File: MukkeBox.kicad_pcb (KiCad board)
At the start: 2 copper layers, 200 x 105 mm, 273 parts, among them J101 Conn_02x20_Odd_Even, J102 Conn_01x04, J103 Conn_02x05_Odd_Even, J104 Conn_02x05_Odd_Even, J201 Conn_02x01, J301 Conn_02x04_Odd_Even, J302 Conn_02x04_Odd_Even, J303 TB001-500-02BE CUI_Devices, J401 TB001-500-02BE CUI_Devices, J501 TB001-500-04BE CUI_Devices, J601 Conn_01x03_Female, J602 Conn_02x01, J603 Conn_02x06_Odd_Even, J604 Conn_02x01, J605 Conn_02x01, Q1 2N7002, Q303 2N7002, Q304 2N7002, Q305 FDD4685-F085, Q306 2N7002, Q307 BSS84, Q308 2N7002, Q309 FDD4685-F085, Q401 2N7002, Q402 2N7002, Q501 2N7002, SW501 DS04-254-2-02BK-SMT, U101 LM35-LP, U102 STM32F030C6Tx_MukkeBox, U201 XC6216C, U202 StepUp, U401 MAX1873TEEE, U501 TDA7498L, U502 BK8000L, U503 TDA7719, U504 AP2553AW6-7, U601 XC6216C, U602 TPS560430, Y101 FOXSDLF/080-20

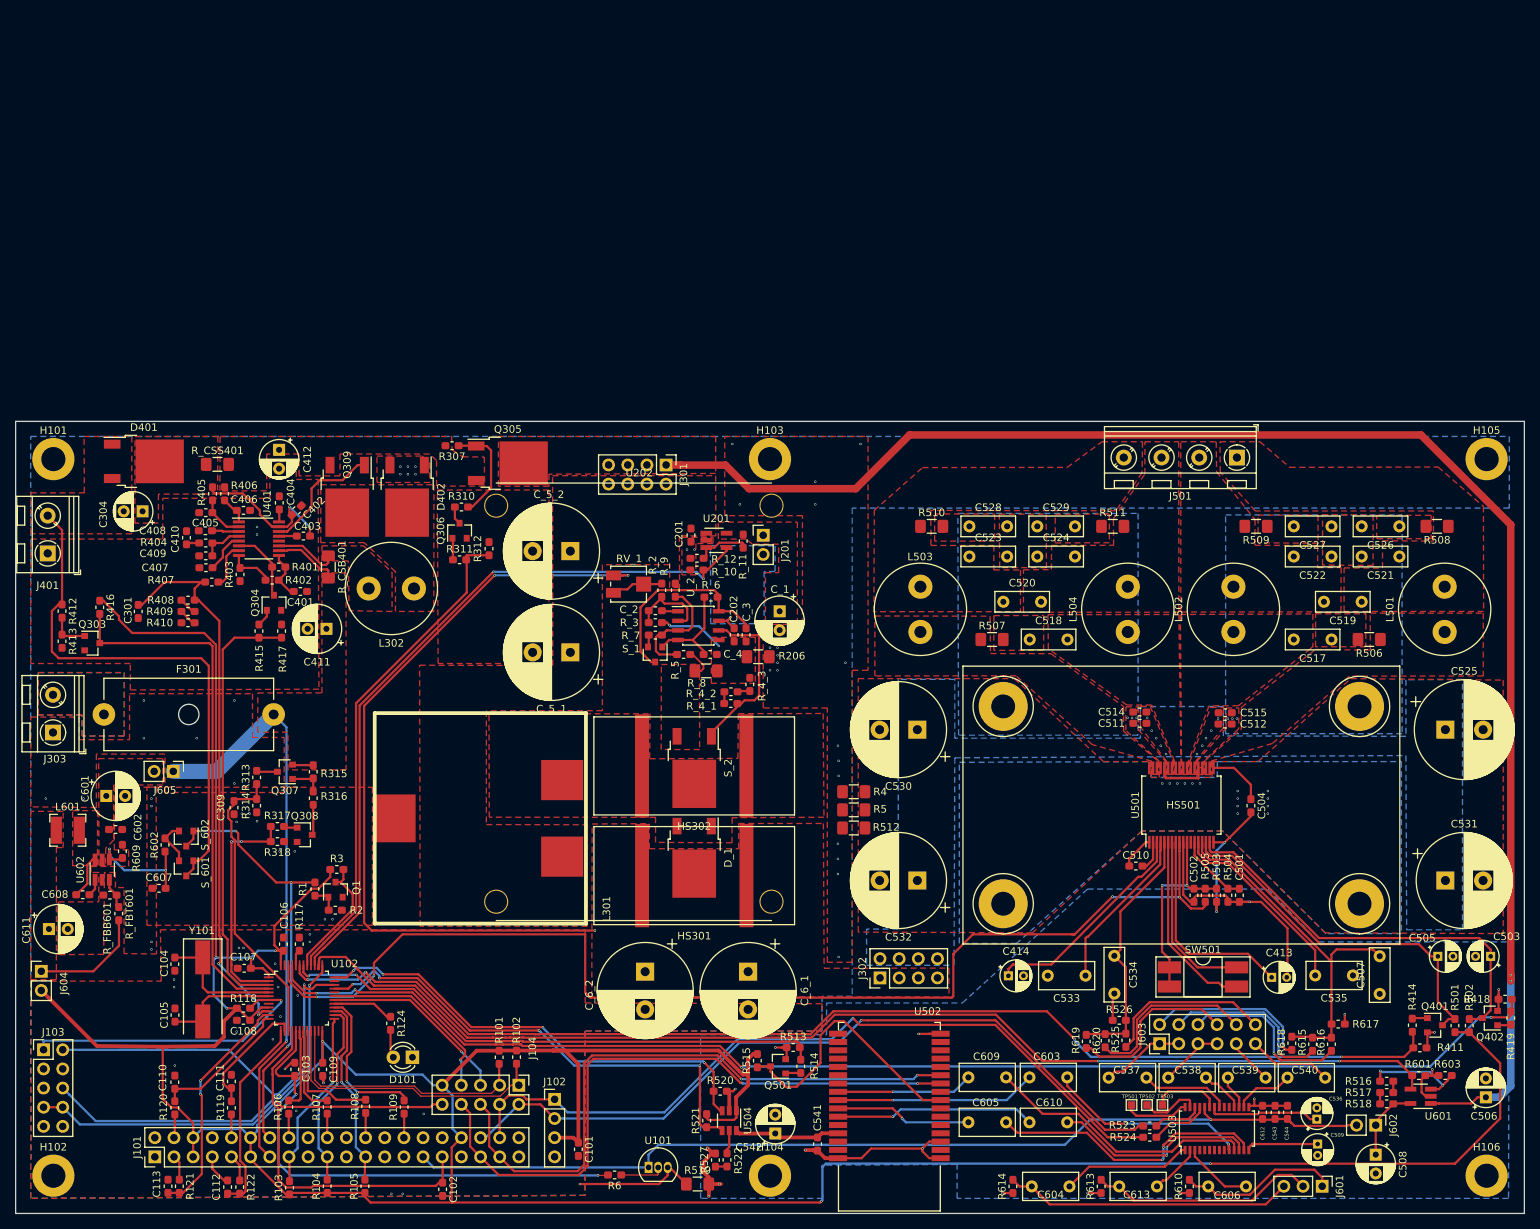
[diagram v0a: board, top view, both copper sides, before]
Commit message: Charger austauschen gegen bq24610
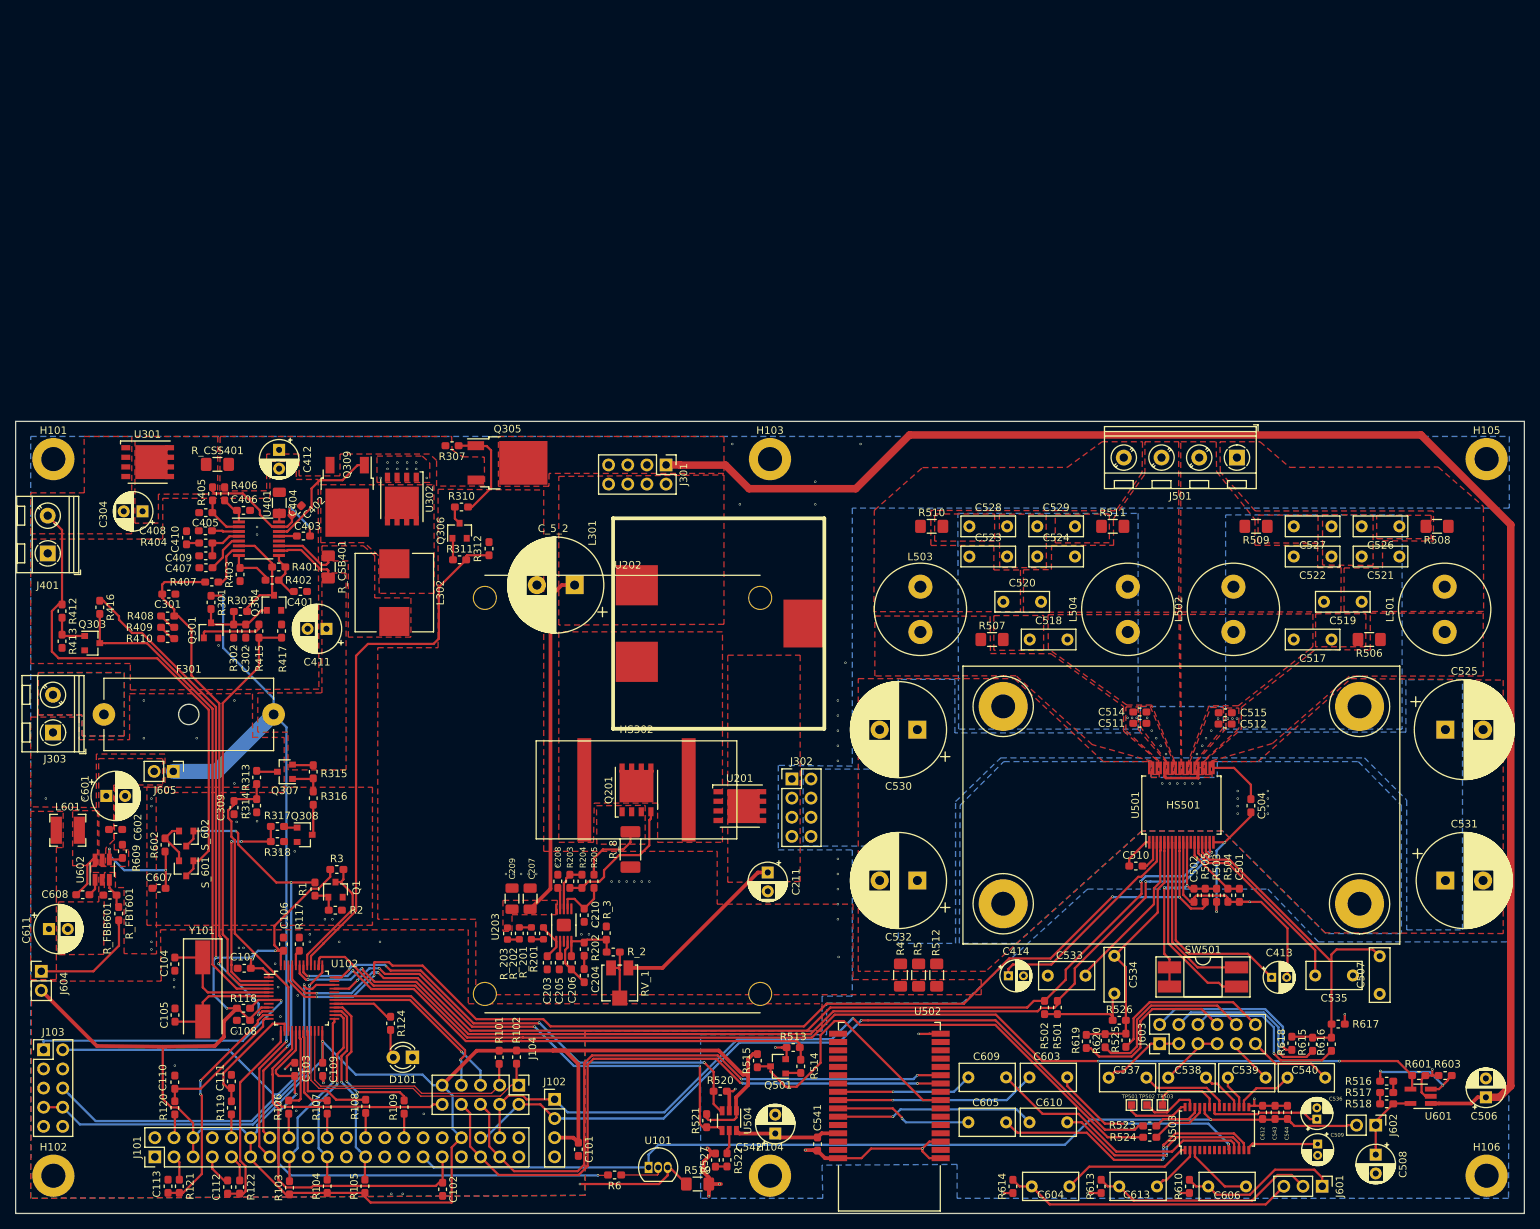
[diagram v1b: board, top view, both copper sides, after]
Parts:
- removed C201, C202: 100n, Capacitor_SMD:C_0603_1608Metric_Pad1.05x0.95mm_HandSolder
- removed C503, C505: 2.2uF 16V, Capacitor_THT:CP_Radial_D4.0mm_P2.00mm
- removed C_1: 68u, Capacitor_THT:CP_Radial_D6.3mm_P2.50mm
- removed C_2: 100nF, Capacitor_SMD:C_0603_1608Metric_Pad1.05x0.95mm_HandSolder
- removed C_3: 220nF, Capacitor_SMD:C_0603_1608Metric_Pad1.05x0.95mm_HandSolder
- removed C_4: 1.2nF, Capacitor_SMD:C_0603_1608Metric_Pad1.05x0.95mm_HandSolder
- removed C_5_1, C_6_1, C_6_2: 560uF 50V, Capacitor_THT:CP_Radial_D12.5mm_P5.00mm
- removed D401, D402, D_1: STPS1045B-TR, Package_TO_SOT_SMD:TO-252-2
- removed HS301: 573300D00000G, Heatsink:Heatsink_AAVID_573300D00010G_TO-263
- removed J201: Conn_02x01, Connector_PinHeader_2.54mm:PinHeader_1x02_P2.54mm_Vertical
- removed Q401, Q402: 2N7002, Package_TO_SOT_SMD:SOT-23
- removed R206: 0R, Resistor_SMD:R_1206_3216Metric_Pad1.42x1.75mm_HandSolder
- removed R411, R418, R_9: 100K, Resistor_SMD:R_0603_1608Metric_Pad1.05x0.95mm_HandSolder
- removed R414, R419, R_5: 1K, Resistor_SMD:R_0603_1608Metric_Pad1.05x0.95mm_HandSolder
- removed R_10, R_12, R_4_1, R_4_2, R_4_3: 10K, Resistor_SMD:R_0603_1608Metric_Pad1.05x0.95mm_HandSolder
- removed R_11: 47K, Resistor_SMD:R_0603_1608Metric_Pad1.05x0.95mm_HandSolder
- removed R_6: 15K, Resistor_SMD:R_0603_1608Metric_Pad1.05x0.95mm_HandSolder
- removed R_7: 5K1, Resistor_SMD:R_0603_1608Metric_Pad1.05x0.95mm_HandSolder
- removed S_1: MMBT2222LT1G, Package_TO_SOT_SMD:SOT-23
- removed S_2: TK7R7P10PL, Package_TO_SOT_SMD:TO-252-2
- removed U_2: UC3843_SOIC8, Package_SO:SOIC-8_3.9x4.9mm_P1.27mm
- added C203: 100p, Capacitor_SMD:C_0603_1608Metric_Pad1.05x0.95mm_HandSolder, F.Cu at (115.9, 108.9)
- added C204: 100n, Capacitor_SMD:C_0603_1608Metric_Pad1.05x0.95mm_HandSolder, F.Cu at (120.8, 110.6)
- added C205: 100n, Capacitor_SMD:C_0603_1608Metric_Pad1.05x0.95mm_HandSolder, F.Cu at (117.5, 108.9)
- added C206: 470p, Capacitor_SMD:C_0603_1608Metric_Pad1.05x0.95mm_HandSolder, F.Cu at (119.1, 108.9)
- added C207: 330n, Capacitor_SMD:C_1206_3216Metric, F.Cu at (113.7, 100.4)
- added C208: 1u, Capacitor_SMD:C_0603_1608Metric_Pad1.05x0.95mm_HandSolder, F.Cu at (117.3, 98.1)
- added C209: 330n, Capacitor_SMD:C_1206_3216Metric, F.Cu at (111.3, 100.4)
- added C210: 220p, Capacitor_SMD:C_0603_1608Metric_Pad1.05x0.95mm_HandSolder, F.Cu at (120.8, 102.6)
- added C211: 68u, Capacitor_THT:CP_Radial_D5.0mm_P2.50mm, F.Cu at (145.2, 96.9)
- added C302: 47n, Capacitor_SMD:C_0603_1608Metric_Pad1.05x0.95mm_HandSolder, F.Cu at (76.0, 64.9)
- added Q201: CSD18504Q5A, Package_TO_SOT_SMD:TDSON-8-1_HandSoldering, F.Cu at (127.8, 85.9)
- added Q301: 2N7002, Package_TO_SOT_SMD:SOT-23, F.Cu at (71.4, 64.8)
- added R201: 100K, Resistor_SMD:R_0603_1608Metric, F.Cu at (115.4, 105.0)
- added R202: 20K, Resistor_SMD:R_0603_1608Metric_Pad1.05x0.95mm_HandSolder, F.Cu at (120.8, 107.1)
- added R203: 22R, Resistor_SMD:R_0603_1608Metric_Pad1.05x0.95mm_HandSolder, F.Cu at (118.9, 98.1)
- added R204: 22R, Resistor_SMD:R_0603_1608Metric_Pad1.05x0.95mm_HandSolder, F.Cu at (120.5, 98.1)
- added R205: 1K, Resistor_SMD:R_0603_1608Metric_Pad1.05x0.95mm_HandSolder, F.Cu at (122.1, 98.1)
- added R301: 1M, Resistor_SMD:R_0603_1608Metric_Pad1.05x0.95mm_HandSolder, F.Cu at (71.4, 61.1)
- added R302: 1M, Resistor_SMD:R_0603_1608Metric_Pad1.05x0.95mm_HandSolder, F.Cu at (74.4, 64.9)
- added R303: DNP, Resistor_SMD:R_0603_1608Metric_Pad1.05x0.95mm_HandSolder, F.Cu at (75.3, 62.3)
- added R_201: 100K, Resistor_SMD:R_0603_1608Metric, F.Cu at (113.8, 105.0)
- added R_202: 100K, Resistor_SMD:R_0603_1608Metric, F.Cu at (112.2, 105.0)
- added R_203: 100K, Resistor_SMD:R_0603_1608Metric, F.Cu at (110.7, 105.0)
- added U203: TPS40210, Package_SO:MSOP-10-1EP_3x3mm_P0.5mm_EP1.68x1.88mm, F.Cu at (118.1, 103.9)
- added U301: STPS30M60DJF, Package_TO_SOT_SMD:TDSON-8-1_HandSoldering, F.Cu at (63.0, 42.5)
- added U302: STPS30M60DJF, Package_TO_SOT_SMD:TDSON-8-1_HandSoldering, F.Cu at (96.7, 47.4)
- C404: value 220n -> 2.2u 30V; footprint Capacitor_SMD:C_0603_1608Metric_Pad1.05x0.95mm_HandSolder -> Capacitor_SMD:C_1206_3216Metric
- L301: value 33uH PQ2617BLA-330K -> 22uH PQ2617BHA-220K
- L302: value 22uH 6100-220K-RC -> 10u Würth 7443251000; footprint Inductor_THT:L_Radial_D12.0mm_P6.00mm_MuRATA_1900R -> Inductor_SMD:L_Wuerth_HCI-1050
- Q305, Q309: value FDD4685-F085 -> FDD5614P
- R307: value 1M -> 100K
- R310: value 1K -> 100K
- R402, R403: value 4.7k 1% -> 100K
- R_2: value 2K94 -> 47K
- R_3: value 1K -> 422R
- R_8: value R010 -> R007; footprint Resistor_SMD:R_1206_3216Metric_Pad1.42x1.75mm_HandSolder -> Resistor_SMD:R_2010_5025Metric_Pad1.52x2.65mm_HandSolder
- R_CSB401: value 200m -> 68m
- U201: value XC6216C -> STPS30M60DJF; footprint Package_TO_SOT_SMD:SOT-23-5_HandSoldering -> Package_TO_SOT_SMD:TDSON-8-1_HandSoldering
- moved R502 56.4 mm to (181.9, 114.8), turned to 90 degrees
- moved RV_1 52.9 mm to (125.5, 111.5), turned to 0 degrees
- moved R501 52.8 mm to (183.6, 114.8), turned to 90 degrees
- moved R_2 48.4 mm to (124.7, 107.4), turned to 0 degrees
- moved L301 46.4 mm to (142.2, 63.9), turned to 270 degrees
- moved R_3 41.7 mm to (123.8, 104.9), turned to 270 degrees
- moved U201 35.4 mm to (141.5, 88.1)
- moved J302 28.8 mm to (148.4, 84.5), turned to 0 degrees
- moved R_8 25.7 mm to (127.0, 93.8), turned to 90 degrees
- moved R4 25.1 mm to (162.8, 110.5), turned to 270 degrees
- moved R5 23.5 mm to (165.2, 110.5), turned to 270 degrees
- moved R512 22.4 mm to (167.6, 110.5), turned to 270 degrees
- moved U202 12.3 mm to (107.7, 60.5)
- moved HS302 8.28 mm to (127.8, 85.9), turned to 0 degrees
- moved C301 4.66 mm to (65.8, 60.0), turned to 0 degrees
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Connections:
- HS302 pad 1: Net-(D_1-Pad1) -> Net-(HS302-Pad1)
- J302 pad 1: Net-(C_6_1-Pad1) -> Net-(C211-Pad1)
- J302 pad 3: Net-(C_6_1-Pad1) -> Net-(C211-Pad1)
- J302 pad 5: Net-(C_6_1-Pad1) -> Net-(C211-Pad1)
- J302 pad 7: Net-(C_6_1-Pad1) -> Net-(C211-Pad1)
- L301 pad 2: Net-(D_1-Pad1) -> Net-(HS302-Pad1)
- Q304 pad 1: Net-(Q304-Pad1) -> Net-(C302-Pad1)
- R415 pad 2: Net-(Q304-Pad1) -> Net-(Q301-Pad1)
- R501 pad 1: Net-(C505-Pad1) -> GNDA
- R501 pad 2: +3V3 -> MUTE_TDA7498
- R502 pad 1: Net-(C503-Pad1) -> GNDA
- R502 pad 2: +3V3 -> STBY_TDA7498
- RV_1 pad 1: Net-(C_6_1-Pad1) -> Net-(C211-Pad1)
- R_3 pad 1: /02_StepUp/STEPUP_GND -> GND
- R_8 pad 1: /02_StepUp/STEPUP_GND -> GND
- U201 pad 1: /02_StepUp/IN_STEPUP -> Net-(HS302-Pad1)
- U201 pad 2: GND -> Net-(HS302-Pad1)
- U201 pad 3: Net-(R_11-Pad2) -> Net-(HS302-Pad1)
- U201 pad 4: ENABLE_12V -> Net-(HS302-Pad1)
- U201 pad 5: Net-(C_1-Pad1) -> Net-(C211-Pad1)
- U501 pad 20: Net-(C503-Pad1) -> STBY_TDA7498
- U501 pad 21: Net-(C505-Pad1) -> MUTE_TDA7498
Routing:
- net +3V3: track 489.2 -> 323.1 mm, vias 7 -> 5
- net Net-(C_6_1-Pad1): track 103.9 -> 0.00 mm, vias 3 -> 0
- net ENABLE_12V: track 95.9 -> 0.00 mm, vias 2 -> 0
- net Net-(C503-Pad1): track 55.1 -> 0.00 mm
- net Net-(C505-Pad1): track 49.0 -> 0.00 mm
- net /02_StepUp/IN_STEPUP: track 0.00 -> 46.4 mm
- net STBY_TDA7498: track 173.8 -> 142.1 mm
- net Net-(C_3-Pad2): track 27.0 -> 0.00 mm
- net Net-(C211-Pad1): track 0.00 -> 23.7 mm
- net Net-(R_4_1-Pad1): track 22.7 -> 0.00 mm
- net PACK+: track 89.4 -> 109.5 mm, vias 1 -> 2
- net MUTE_TDA7498: track 159.5 -> 141.0 mm
- net Net-(Q201-Pad4): track 0.00 -> 17.9 mm
- net /02_StepUp/STEPUP_CS: track 15.7 -> 0.00 mm
- net Net-(C_4-Pad1): track 13.2 -> 0.00 mm
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- added copper zone on F.Cu, net Net-(C211-Pad1)
- added copper zone on F.Cu, net Net-(HS302-Pad1)
- removed copper zone on B.Cu, net /02_StepUp/12V
- removed copper zone on F.Cu, net /02_StepUp/STEPUP_GND
- removed copper zone on F.Cu, net Net-(C_1-Pad1)
- removed copper zone on F.Cu, net Net-(C_6_1-Pad1)
- removed copper zone on F.Cu, net Net-(D_1-Pad1)

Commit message: Charger ausgetauscht, Mosfet und Dioden durch billigere ersetzt
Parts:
- removed C401: 1u, Capacitor_SMD:C_0603_1608Metric_Pad1.05x0.95mm_HandSolder
- removed C402, C403, C405, C406, C410: 100n, Capacitor_SMD:C_0603_1608Metric_Pad1.05x0.95mm_HandSolder
- removed C404: 2.2u 30V, Capacitor_SMD:C_1206_3216Metric
- removed C407, C408: 47n, Capacitor_SMD:C_0603_1608Metric_Pad1.05x0.95mm_HandSolder
- removed C409: 1n, Capacitor_SMD:C_0603_1608Metric_Pad1.05x0.95mm_HandSolder
- removed R401: 100k, Resistor_SMD:R_0603_1608Metric_Pad1.05x0.95mm_HandSolder
- removed R402, R403: 100K, Resistor_SMD:R_0603_1608Metric_Pad1.05x0.95mm_HandSolder
- removed R404: 10k, Resistor_SMD:R_0603_1608Metric_Pad1.05x0.95mm_HandSolder
- removed R405, R406: 4.7k, Resistor_SMD:R_0603_1608Metric_Pad1.05x0.95mm_HandSolder
- removed R407, R408, R409, R410: 1K, Resistor_SMD:R_0603_1608Metric_Pad1.05x0.95mm_HandSolder
- removed R_CSB401: 68m, Resistor_SMD:R_1206_3216Metric_Pad1.42x1.75mm_HandSolder
- removed R_CSS401: 33m, Resistor_SMD:R_1206_3216Metric_Pad1.42x1.75mm_HandSolder
- removed S_601, S_602: MMBT2222LT1G, Package_TO_SOT_SMD:SOT-23
- removed U201, U302: STPS30M60DJF, Package_TO_SOT_SMD:TDSON-8-1_HandSoldering
- removed U401: MAX1873TEEE, Package_SO:QSOP-16_3.9x4.9mm_P0.635mm
- added C15C301: 100n, Capacitor_SMD:C_0603_1608Metric_Pad1.05x0.95mm_HandSolder, F.Cu at (64.2, -5.69)
- added C303: 100n, Capacitor_SMD:C_0603_1608Metric_Pad1.05x0.95mm_HandSolder, F.Cu at (68.7, -10.4)
- added C305: 100n, Capacitor_SMD:C_0603_1608Metric_Pad1.05x0.95mm_HandSolder, F.Cu at (70.0, -14.3)
- added C306: 100n, Capacitor_SMD:C_0603_1608Metric_Pad1.05x0.95mm_HandSolder, F.Cu at (60.4, -3.65)
- added C307: 1u, Capacitor_SMD:C_1210_3225Metric, F.Cu at (61.7, -13.4)
- added C308: 33n, Capacitor_SMD:C_0603_1608Metric_Pad1.05x0.95mm_HandSolder, F.Cu at (65.3, -8.90)
- added C310: 1u, Capacitor_SMD:C_1210_3225Metric, F.Cu at (56.8, -8.83)
- added C311: 33n, Capacitor_SMD:C_0603_1608Metric_Pad1.05x0.95mm_HandSolder, F.Cu at (64.2, -7.20)
- added C312: 100n, Capacitor_SMD:C_0603_1608Metric_Pad1.05x0.95mm_HandSolder, F.Cu at (65.3, -10.4)
- added C313: 100n, Capacitor_SMD:C_0603_1608Metric_Pad1.05x0.95mm_HandSolder, F.Cu at (70.0, -12.8)
- added C314: 22p, Capacitor_SMD:C_0603_1608Metric_Pad1.05x0.95mm_HandSolder, F.Cu at (68.7, -8.90)
- added D201: PS1060L, Package_TO_SOT_SMD:TO-277B, F.Cu at (82.5, -11.1)
- added D301: BAT54C, Package_TO_SOT_SMD:SOT-23, F.Cu at (60.8, -6.18)
- added D601: BAT54C, Package_TO_SOT_SMD:SOT-23, F.Cu at (56.2, 2.55)
- added Q202: VS6412AE, Package_SON:Diodes_PowerDI3333-8, F.Cu at (86.8, -13.1)
- added Q302: HSBB3103, Package_SON:Diodes_PowerDI3333-8, F.Cu at (66.2, -13.1)
- added Q310: HSBB3103, Package_SON:Diodes_PowerDI3333-8, F.Cu at (56.6, -5.30)
- added Q311: HSBB3103, Package_SON:Diodes_PowerDI3333-8, F.Cu at (61.5, -9.88)
- added R15C301: 100K, Resistor_SMD:R_0603_1608Metric_Pad1.05x0.95mm_HandSolder, F.Cu at (74.3, -8.22)
- added R19C301: 100K, Resistor_SMD:R_0603_1608Metric_Pad1.05x0.95mm_HandSolder, F.Cu at (70.4, -4.37)
- added R1C301: 100K, Resistor_SMD:R_0603_1608Metric_Pad1.05x0.95mm_HandSolder, F.Cu at (70.9, -5.88)
- added R2C301: 700K, Resistor_SMD:R_0603_1608Metric_Pad1.05x0.95mm_HandSolder, F.Cu at (75.4, -9.73)
- added R304: 100K, Resistor_SMD:R_0603_1608Metric_Pad1.05x0.95mm_HandSolder, F.Cu at (70.9, -7.39)
- added R305: 100K, Resistor_SMD:R_0603_1608Metric_Pad1.05x0.95mm_HandSolder, F.Cu at (73.3, -14.3)
- added R306: 100K, Resistor_SMD:R_0603_1608Metric_Pad1.05x0.95mm_HandSolder, F.Cu at (73.8, -4.37)
- added R308: 10R, Resistor_SMD:R_0603_1608Metric_Pad1.05x0.95mm_HandSolder, F.Cu at (74.3, -6.71)
- added R3C301: 100K, Resistor_SMD:R_0603_1608Metric_Pad1.05x0.95mm_HandSolder, F.Cu at (75.4, -11.2)
- added R4C301: 22K, Resistor_SMD:R_0603_1608Metric_Pad1.05x0.95mm_HandSolder, F.Cu at (63.7, -3.65)
- added R5C301: 100K, Resistor_SMD:R_0603_1608Metric_Pad1.05x0.95mm_HandSolder, F.Cu at (67.1, -4.18)
- added R6C301: 10K, Resistor_SMD:R_0603_1608Metric_Pad1.05x0.95mm_HandSolder, F.Cu at (67.6, -5.88)
- added R7C301: 100K, Resistor_SMD:R_0603_1608Metric_Pad1.05x0.95mm_HandSolder, F.Cu at (72.0, -9.73)
- added R8C301: 10K, Resistor_SMD:R_0603_1608Metric_Pad1.05x0.95mm_HandSolder, F.Cu at (73.3, -12.8)
- added R9C301: 2K2, Resistor_SMD:R_0603_1608Metric_Pad1.05x0.95mm_HandSolder, F.Cu at (72.0, -11.2)
- added R9C302: 6K8, Resistor_SMD:R_0603_1608Metric_Pad1.05x0.95mm_HandSolder, F.Cu at (67.6, -7.39)
- added RAC301: 10m, Resistor_SMD:R_1206_3216Metric_Pad1.42x1.75mm_HandSolder, F.Cu at (56.9, -11.6)
- added RSR301: 10m, Resistor_SMD:R_1206_3216Metric_Pad1.42x1.75mm_HandSolder, F.Cu at (56.9, -13.9)
- C302: value 47n -> 100n
- C304: value 68u -> 1u; footprint Capacitor_THT:CP_Radial_D5.0mm_P2.50mm -> Capacitor_SMD:C_1210_3225Metric
- C411: value 68u -> 10u
- Q201: value CSD18504Q5A -> VS6412AE; footprint Package_TO_SOT_SMD:TDSON-8-1_HandSoldering -> Package_SON:Diodes_PowerDI3333-8
- Q304: value 2N7002 -> HSBB3103; footprint Package_TO_SOT_SMD:SOT-23 -> Package_SON:Diodes_PowerDI3333-8
- Q305, Q309: value FDD5614P -> VS6412AE; footprint Package_TO_SOT_SMD:TO-252-2 -> Package_SON:Diodes_PowerDI3333-8
- R301, R302: value 1M -> 100K
- R303: value DNP -> 100K
- U301: value STPS30M60DJF -> BQ24610; footprint Package_TO_SOT_SMD:TDSON-8-1_HandSoldering -> Package_DFN_QFN:VQFN-24-1EP_4x4mm_P0.5mm_EP2.45x2.45mm_ThermalVias
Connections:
- C301 pad 1: CHARGER_IOUT -> Net-(C301-Pad1)
- C301 pad 2: GND -> Net-(C301-Pad2)
- C302 pad 1: Net-(C302-Pad1) -> GND
- C302 pad 2: GND -> /00_Charger/CE
- C304 pad 1: /00_Charger/POWER_SUPPLY -> GND
- C304 pad 2: GND -> /00_Charger/VREF
- C412 pad 1: Net-(C412-Pad1) -> Net-(C15C301-Pad2)
- L302 pad 2: Net-(L302-Pad2) -> /00_Charger/SRP
- Q301 pad 3: Net-(C302-Pad1) -> /00_Charger/CE
- Q304 pad 1: Net-(C302-Pad1) -> Net-(C301-Pad2)
- Q304 pad 2: GND -> Net-(C301-Pad2)
- Q304 pad 3: Net-(Q304-Pad3) -> Net-(C301-Pad2)
- Q305 pad 1: Net-(Q305-Pad1) -> Net-(L302-Pad1)
- Q305 pad 2: SYSTEM_LOAD -> Net-(L302-Pad1)
- Q305 pad 3: Net-(C412-Pad1) -> Net-(L302-Pad1)
- Q309 pad 1: Net-(Q309-Pad1) -> GND
- Q309 pad 2: Net-(L302-Pad1) -> GND
- Q309 pad 3: Net-(C412-Pad1) -> GND
- R203 pad 2: Net-(Q201-Pad4) -> Net-(Q202-Pad4)
- R301 pad 1: PACK+ -> +3V3
- R301 pad 2: Net-(C302-Pad1) -> CHARGER_PG
- R302 pad 1: Net-(C302-Pad1) -> /00_Charger/VREF
- R302 pad 2: GND -> /00_Charger/CE
- R303 pad 1: Net-(C302-Pad1) -> +3V3
- R303 pad 2: Net-(Q304-Pad3) -> CHARGER_STAT2
- R307 pad 1: Net-(Q305-Pad1) -> Net-(Q311-Pad4)
- R307 pad 2: Net-(C412-Pad1) -> Net-(C15C301-Pad2)
- R310 pad 2: Net-(Q305-Pad1) -> Net-(Q311-Pad4)
- U102 pad 10: CHARGER_IOUT -> CHARGER_PG
- U102 pad 32: Net-(U102-Pad32) -> CHARGER_STAT1
- U102 pad 35: Net-(U102-Pad35) -> CHARGER_STAT2
- U301 pad 1: DC_20V_POWER_SUPPLY -> Net-(C15C301-Pad2)
- U301 pad 2: DC_20V_POWER_SUPPLY -> Net-(C303-Pad2)
- U301 pad 3: DC_20V_POWER_SUPPLY -> Net-(R306-Pad1)
- U301 pad 4: DC_20V_POWER_SUPPLY -> /00_Charger/CE
- U301 pad 5: /00_Charger/POWER_SUPPLY -> CHARGER_STAT1
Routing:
- net Net-(Q311-Pad4): track 0.00 -> 13.6 mm
- net Net-(Q305-Pad1): track 13.6 -> 0.00 mm
- net Net-(L302-Pad2): track 8.63 -> 0.00 mm
- net /00_Charger/SRP: track 0.00 -> 8.63 mm
- added copper zone on F.Cu, net /00_Charger/SRP
- added copper zone on F.Cu, net Net-(HS302-Pad1)
- removed copper zone on F.Cu, net Net-(D201-Pad1)
- removed copper zone on F.Cu, net Net-(L302-Pad2)
